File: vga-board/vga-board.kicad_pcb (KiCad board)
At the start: 2 copper layers, 24 parts, among them U1 74HC244, U10 74HC163, U11 74LS158, U12 74LS251, U13 74HC244, U14 74HC244, U15 74HC244, U16 GAL22V10, U17 GAL22V10, U18 GAL22V10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

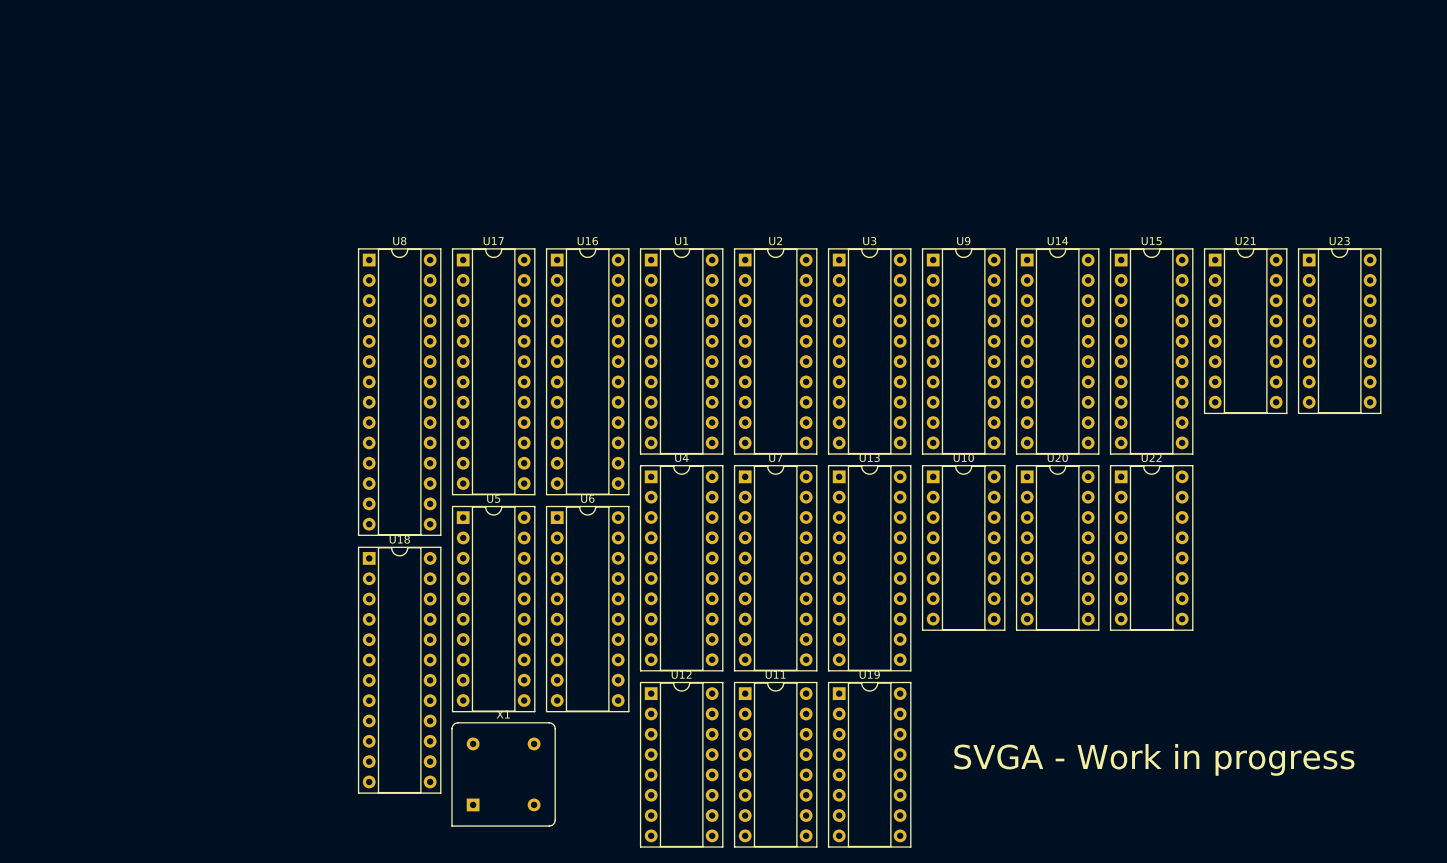
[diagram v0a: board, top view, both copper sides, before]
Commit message: Integtrate IO into mail board, begion VGA layout
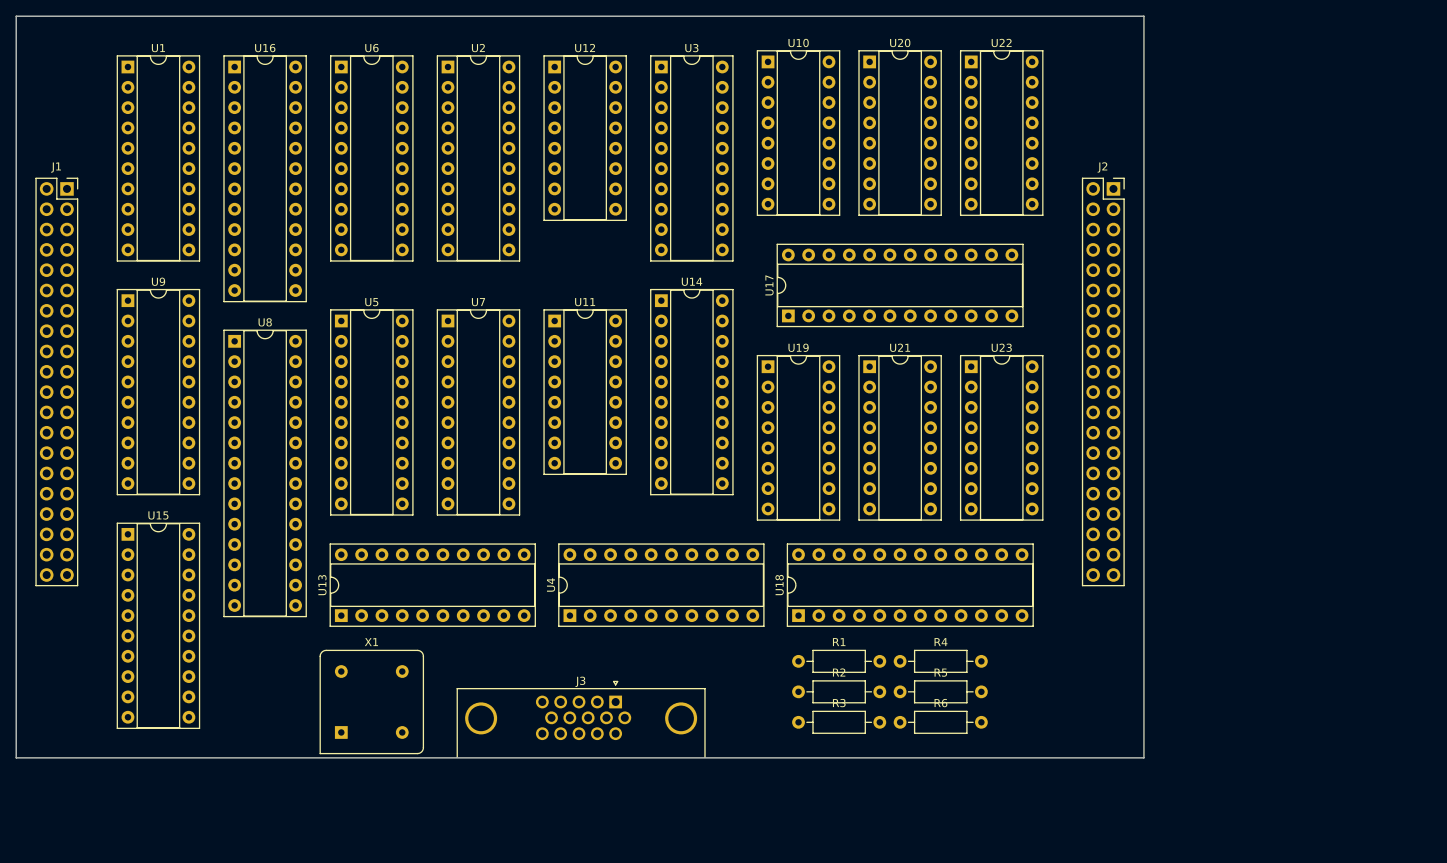
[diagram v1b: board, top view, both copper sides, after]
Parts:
- added J1: Conn_02x20_Odd_Even, Connector_PinSocket_2.54mm:PinSocket_2x20_P2.54mm_Vertical, F.Cu at (87.0, 63.5)
- added J2: Conn_02x20_Odd_Even, Connector_PinSocket_2.54mm:PinSocket_2x20_P2.54mm_Vertical, F.Cu at (217.8, 63.5)
- added J3: DB15_Female_HighDensity, Connector_Dsub:DSUB-15-HD_Female_Horizontal_P2.29x1.98mm_EdgePinOffset3.03mm_Housed_MountingHolesOffset4.94mm, F.Cu at (155.6, 127.6)
- added R1: 680R, Resistor_THT:R_Axial_DIN0207_L6.3mm_D2.5mm_P10.16mm_Horizontal, F.Cu at (178.4, 122.6)
- added R2: 680R, Resistor_THT:R_Axial_DIN0207_L6.3mm_D2.5mm_P10.16mm_Horizontal, F.Cu at (178.4, 126.4)
- added R3: 680R, Resistor_THT:R_Axial_DIN0207_L6.3mm_D2.5mm_P10.16mm_Horizontal, F.Cu at (178.4, 130.2)
- added R4: 1.2k, Resistor_THT:R_Axial_DIN0207_L6.3mm_D2.5mm_P10.16mm_Horizontal, F.Cu at (191.1, 122.6)
- added R5: 1.2k, Resistor_THT:R_Axial_DIN0207_L6.3mm_D2.5mm_P10.16mm_Horizontal, F.Cu at (191.1, 126.4)
- added R6: 1.2k, Resistor_THT:R_Axial_DIN0207_L6.3mm_D2.5mm_P10.16mm_Horizontal, F.Cu at (191.1, 130.2)
- moved U15 128.8 mm to (94.6, 106.7)
- moved U9 100.8 mm to (94.6, 77.5)
- moved U12 79.3 mm to (148.0, 48.3)
- moved U1 69.7 mm to (94.6, 48.3)
- moved U13 64.6 mm to (121.3, 116.8), turned to 90 degrees
- moved U6 62.5 mm to (121.3, 48.3)
- moved U10 55.8 mm to (174.6, 47.6)
- moved U20 55.5 mm to (187.3, 47.6)
- moved U22 55.1 mm to (200.0, 47.6)
- moved U18 54.1 mm to (178.4, 116.8), turned to 90 degrees
- moved U11 52.3 mm to (148.0, 80.0)
- moved U16 47.0 mm to (108.0, 48.3)
- moved U14 46.0 mm to (161.3, 77.5)
- moved U21 45.2 mm to (187.3, 85.7)
- moved U23 44.3 mm to (200.0, 85.7)
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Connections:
- net VBLANK renamed Net-(U18-Pad18)
- U17 pad 1: X0 -> VCLK
- U17 pad 10: X9 -> X8
- U17 pad 11: X10 -> X9
- U17 pad 13: Net-(U17-Pad13) -> X10
- U17 pad 16: LINE_INC -> Net-(U17-Pad16)
- U17 pad 17: !HRST -> Net-(U17-Pad17)
- U17 pad 18: HBLANK -> Net-(U17-Pad18)
- U17 pad 19: HSYNC -> Net-(U17-Pad19)
- U17 pad 2: X1 -> X0
- U17 pad 20: HBLANK_END -> LINE_INC
- U17 pad 21: HBLANK_START -> !HRST
- U17 pad 22: HSYNC_END -> HBLANK
- U17 pad 23: HSYNC_START -> HSYNC
- U17 pad 3: CLK -> X1
- U17 pad 4: X3 -> CLK
- U17 pad 5: X4 -> X3
- U17 pad 6: X5 -> X4
- U17 pad 7: X6 -> X5
- U17 pad 8: X7 -> X6
- U17 pad 9: X8 -> X7
- U18 pad 1: Y0 -> VCLK
- U18 pad 10: Y9 -> Y8
- U18 pad 11: Y10 -> Y9
- U18 pad 13: HBLANK -> Y10
- U18 pad 16: BLANK -> Net-(U18-Pad16)
- U18 pad 17: !VRST -> Net-(U18-Pad17)
- U18 pad 19: VSYNC -> Net-(U18-Pad19)
- U18 pad 2: Y1 -> Y0
- U18 pad 20: VBLANK_END -> !VRST
- U18 pad 21: VBLANK_START -> BLANK
- U18 pad 22: VSYNC_END -> VSYNC
- U18 pad 23: VSYNC_START -> HBLANK
- U18 pad 3: Y2 -> Y1
- U18 pad 4: Y3 -> Y2
- U18 pad 5: Y4 -> Y3
- U18 pad 6: Y5 -> Y4
- U18 pad 7: Y6 -> Y5
- U18 pad 8: Y7 -> Y6
- U18 pad 9: Y8 -> Y7
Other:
- board outline added: 141 x 92.7 mm
- net class Wide added: clearance 0.2, trace_width 0.5, via_dia 0.8, via_drill 0.4
- board text removed: "SVGA - Work in progress"

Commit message: Revert "Integtrate IO into mail board, begion VGA layout"
This reverts commit 15baf3f71fbe492a9e0b6e5b5ec863db56e31855.
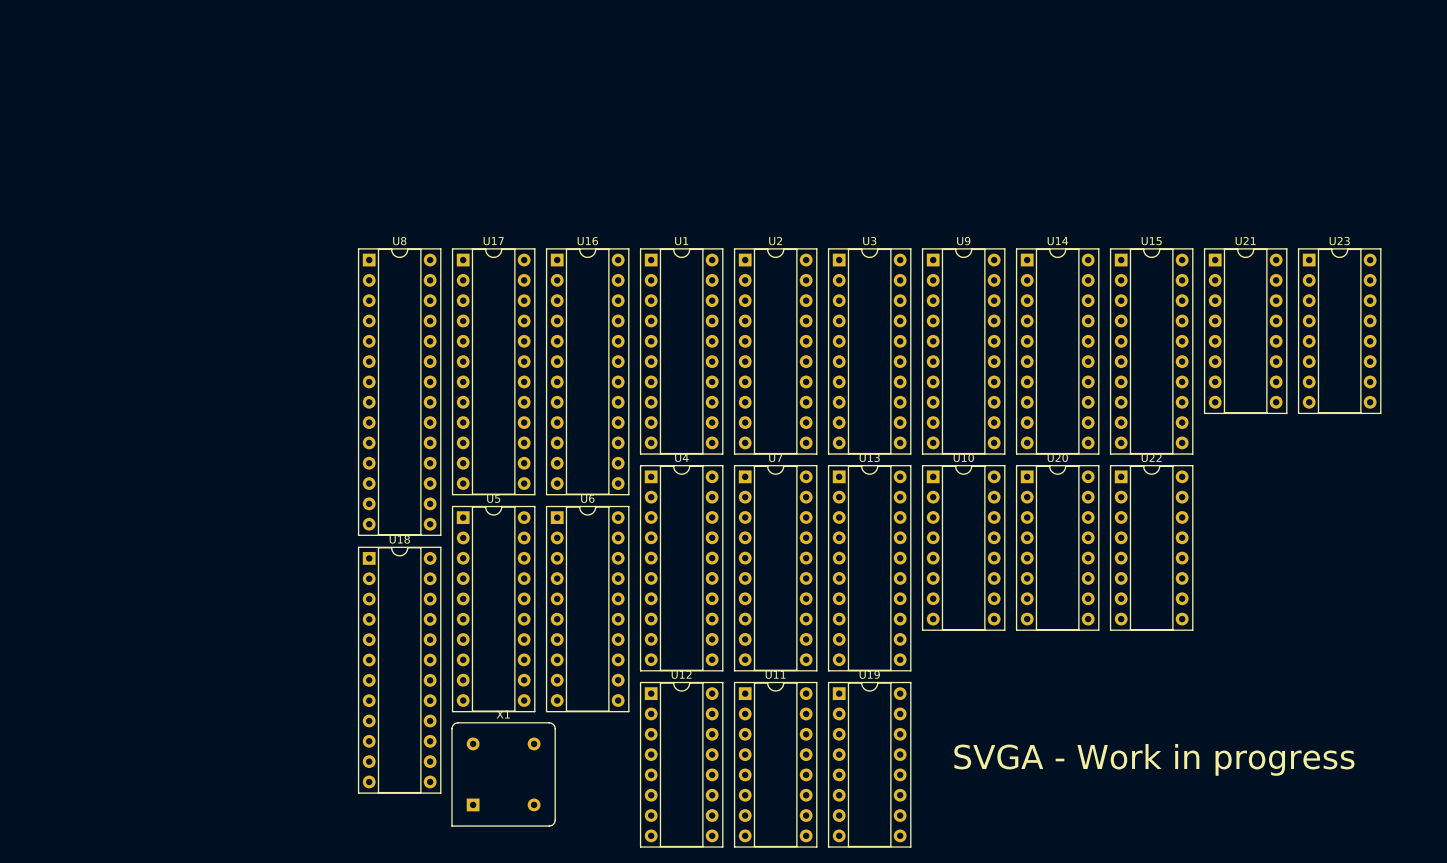
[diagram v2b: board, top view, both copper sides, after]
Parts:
- removed J1, J2: Conn_02x20_Odd_Even, Connector_PinSocket_2.54mm:PinSocket_2x20_P2.54mm_Vertical
- removed J3: DB15_Female_HighDensity, Connector_Dsub:DSUB-15-HD_Female_Horizontal_P2.29x1.98mm_EdgePinOffset3.03mm_Housed_MountingHolesOffset4.94mm
- removed R1, R2, R3: 680R, Resistor_THT:R_Axial_DIN0207_L6.3mm_D2.5mm_P10.16mm_Horizontal
- removed R4, R5, R6: 1.2k, Resistor_THT:R_Axial_DIN0207_L6.3mm_D2.5mm_P10.16mm_Horizontal
- moved U15 128.8 mm to (218.8, 72.4)
- moved U9 100.8 mm to (195.3, 72.4)
- moved U12 79.3 mm to (160.0, 126.6)
- moved U1 69.7 mm to (160.0, 72.4)
- moved U13 64.6 mm to (183.5, 99.5), turned to 0 degrees
- moved U6 62.5 mm to (148.3, 104.6)
- moved U10 55.8 mm to (195.3, 99.5)
- moved U20 55.5 mm to (207.0, 99.5)
- moved U22 55.1 mm to (218.8, 99.5)
- moved U18 54.1 mm to (124.8, 109.7), turned to 0 degrees
- moved U11 52.3 mm to (171.8, 126.6)
- moved U16 47.0 mm to (148.3, 72.4)
- moved U14 46.0 mm to (207.0, 72.4)
- moved U21 45.2 mm to (230.5, 72.4)
- moved U23 44.3 mm to (242.3, 72.4)
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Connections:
- net Net-(U18-Pad18) renamed VBLANK
- U17 pad 1: VCLK -> X0
- U17 pad 10: X8 -> X9
- U17 pad 11: X9 -> X10
- U17 pad 13: X10 -> Net-(U17-Pad13)
- U17 pad 16: Net-(U17-Pad16) -> LINE_INC
- U17 pad 17: Net-(U17-Pad17) -> !HRST
- U17 pad 18: Net-(U17-Pad18) -> HBLANK
- U17 pad 19: Net-(U17-Pad19) -> HSYNC
- U17 pad 2: X0 -> X1
- U17 pad 20: LINE_INC -> HBLANK_END
- U17 pad 21: !HRST -> HBLANK_START
- U17 pad 22: HBLANK -> HSYNC_END
- U17 pad 23: HSYNC -> HSYNC_START
- U17 pad 3: X1 -> CLK
- U17 pad 4: CLK -> X3
- U17 pad 5: X3 -> X4
- U17 pad 6: X4 -> X5
- U17 pad 7: X5 -> X6
- U17 pad 8: X6 -> X7
- U17 pad 9: X7 -> X8
- U18 pad 1: VCLK -> Y0
- U18 pad 10: Y8 -> Y9
- U18 pad 11: Y9 -> Y10
- U18 pad 13: Y10 -> HBLANK
- U18 pad 16: Net-(U18-Pad16) -> BLANK
- U18 pad 17: Net-(U18-Pad17) -> !VRST
- U18 pad 19: Net-(U18-Pad19) -> VSYNC
- U18 pad 2: Y0 -> Y1
- U18 pad 20: !VRST -> VBLANK_END
- U18 pad 21: BLANK -> VBLANK_START
- U18 pad 22: VSYNC -> VSYNC_END
- U18 pad 23: HBLANK -> VSYNC_START
- U18 pad 3: Y1 -> Y2
- U18 pad 4: Y2 -> Y3
- U18 pad 5: Y3 -> Y4
- U18 pad 6: Y4 -> Y5
- U18 pad 7: Y5 -> Y6
- U18 pad 8: Y6 -> Y7
- U18 pad 9: Y7 -> Y8
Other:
- board outline removed
- net class Wide removed
- board text added: "SVGA - Work in progress"
